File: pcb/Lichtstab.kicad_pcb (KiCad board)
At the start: 2 copper layers, 100.5 x 87.7 mm, 141 parts, among them CON1 MIKROBUS_HOST_CONN, CON2 MIKROBUS_MODULECONN, J1 RJ45_LED_Shielded, Q1 AO3407A, SW1 TS-1187A-B-A-B, SW2 TS-1187A-B-A-B, U1 ESP32-WROOM-32UE-N4, U10 HL2304, U11 LIS2DH12, U12 LIS2MDLTR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

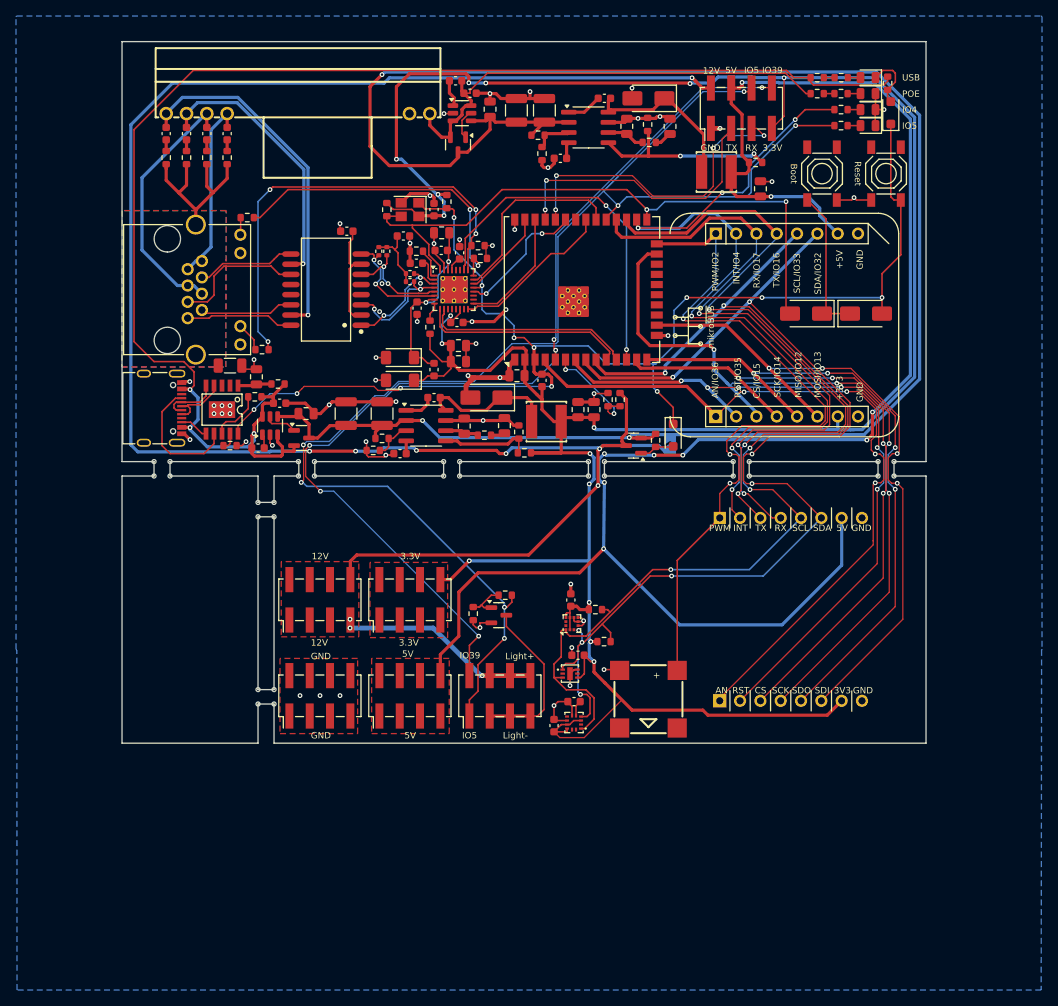
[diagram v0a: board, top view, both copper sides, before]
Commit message: 4 layer pcb
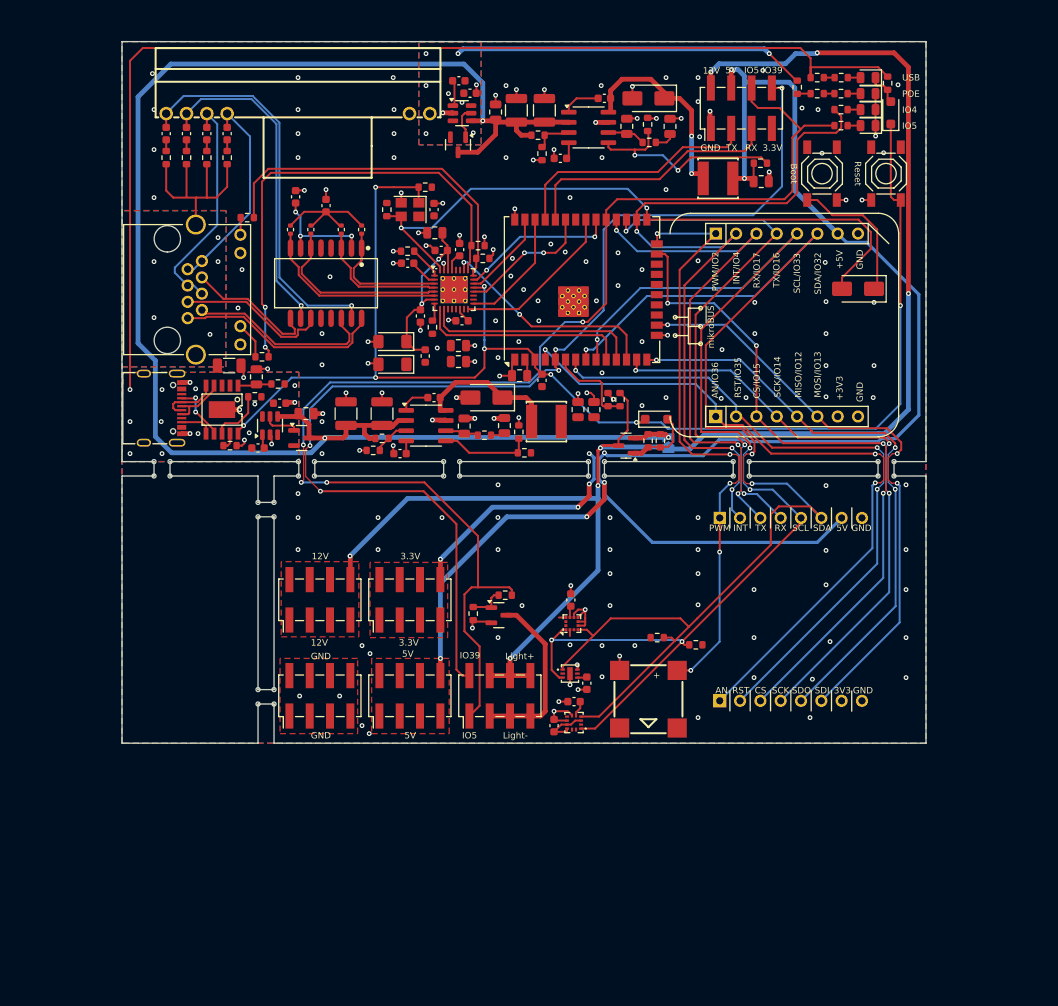
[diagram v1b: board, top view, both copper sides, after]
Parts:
- removed D1: SS34, Diode_SMD:D_SMA
- added R44: 1kΩ, Resistor_SMD:R_0603_1608Metric, F.Cu at (135.8, 98.9)
- added R45: 2.49kΩ, Resistor_SMD:R_0603_1608Metric, F.Cu at (152.9, 54.7)
- moved R41 13.3 mm to (140.2, 124.4), turned to 180 degrees
- moved R9 11.4 mm to (89.6, 72.5)
- moved R11 10.8 mm to (95.9, 72.5), turned to -90 degrees
- moved C14 10.4 mm to (94.0, 69.5), turned to -90 degrees
- moved R10 9.88 mm to (92.1, 72.5)
- moved R13 8.18 mm to (98.5, 72.5), turned to -90 degrees
- moved C11 7.71 mm to (90.2, 68.4), turned to -90 degrees
- moved D2 7.20 mm to (160.5, 79.9)
- moved R40 6.67 mm to (135.4, 123.5)
- moved C42 3.67 mm to (126.6, 129.2), turned to 90 degrees
- moved R1 3.24 mm to (106.4, 67.2), turned to 0 degrees
- moved D9 2.90 mm to (135.3, 96.2), turned to 0 degrees
- moved D5 2.21 mm to (102.3, 89.3)
- moved D6 2.21 mm to (102.3, 86.5)
- moved L2 2.02 mm to (106.4, 88.3)
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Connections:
- net USB_EN renamed /General/ESP_EN
- R34 pad 1: +12V_POE -> Net-(R34-Pad1)
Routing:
- net +3.3V: track 361.1 -> 44.6 mm, vias 16 -> 83
- net +12V: track 263.4 -> 197.0 mm, vias 10 -> 7
- net GND: track 145.0 -> 102.9 mm, vias 58 -> 102
- net +12V_USB: track 176.9 -> 141.2 mm, vias 3 -> 11
- net +12V?: track 240.0 -> 210.4 mm
- net +5V: track 220.4 -> 197.2 mm, vias 9 -> 6
- net /General/EMAC_CRS_DV: track 44.5 -> 28.2 mm
- net /General/ESP_IO39: track 126.2 -> 142.3 mm, vias 6 -> 5
- net /General/ESP_IO2: track 91.7 -> 76.0 mm, vias 3 -> 5
- net /General/ESP_IO16: track 85.3 -> 69.9 mm
- net +12V_POE: track 59.5 -> 44.3 mm, vias 0 -> 8
- net /General/ESP_IO17: track 81.4 -> 66.8 mm
- net /General/I2C_SDA: track 145.1 -> 157.2 mm, vias 8 -> 3
- net /POE/TX+: track 13.4 -> 25.2 mm
- net /POE/TX-: track 11.6 -> 22.8 mm
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- added copper zone on B.Cu, net +12V_POE
- added copper zone on F.Cu, net +12V_POE
- added copper zone on B.Cu, net +12V_USB
- added copper zone on F.Cu, net +12V_USB
- added copper zone on B.Cu, net +3.3V
- added copper zone on In1.Cu, net GND
- added copper zone on In2.Cu, net GND
- added copper zone on In1.Cu, net Net-(C4-Pad2)
- added copper zone on In2.Cu, net Net-(C4-Pad2)
- removed copper zone on B.Cu, net GND
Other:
- copper layers 2 -> 4
- board text added: "Lichtstab Module v0.4"
- board text added: "Lichtstab v0.4"
- board text removed: "Lichtstab Module v0.3"
- board text removed: "Lichtstab v0.3"

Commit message: add mounting holes
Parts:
- added REF**: MountingHole_2mm, MountingHole:MountingHole_2mm, F.Cu at (70.7, 105.5)
- added REF**: MountingHole_2mm, MountingHole:MountingHole_2mm, F.Cu at (89.7, 105.5)
- added REF**: MountingHole_2mm, MountingHole:MountingHole_2mm, F.Cu at (70.8, 51.2)
- added REF**: MountingHole_2mm, MountingHole:MountingHole_2mm, F.Cu at (160.8, 84.7)
- added REF**: MountingHole_2mm, MountingHole:MountingHole_2mm, F.Cu at (70.8, 134.4)
- added REF**: MountingHole_2mm, MountingHole:MountingHole_2mm, F.Cu at (166.2, 51.8)
- added REF**: MountingHole_2mm, MountingHole:MountingHole_2mm, F.Cu at (166.7, 134.4)
- moved D8 1.20 mm to (164.6, 59.1)
- moved R32 1.00 mm to (164.2, 55.2)
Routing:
- net +12V_USB: track 141.2 -> 139.1 mm
- net +12V: track 197.0 -> 195.4 mm
- net /General/ESP_EN: track 172.9 -> 172.2 mm
- net +3.3V: vias 83 -> 82

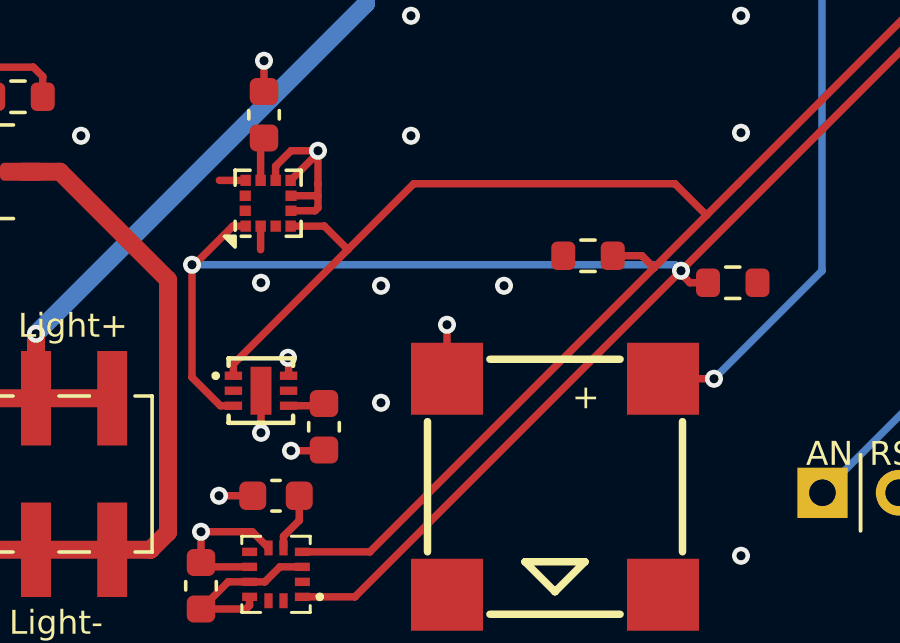
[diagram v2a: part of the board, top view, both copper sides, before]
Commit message: fix GXHTC3C pinout
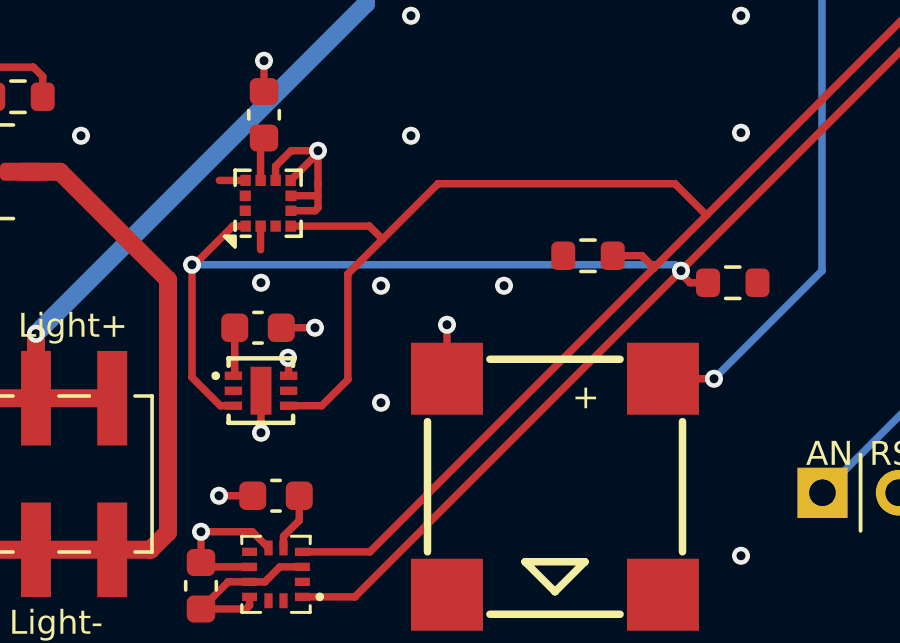
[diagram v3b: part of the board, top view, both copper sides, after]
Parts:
- moved C42 3.97 mm to (124.4, 125.9), turned to 180 degrees
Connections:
- U15 pad 1: /General/I2C_SDA -> +3.3V
- U15 pad 4: +3.3V -> /General/I2C_SDA
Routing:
- net /General/I2C_SDA: track 157.2 -> 158.6 mm
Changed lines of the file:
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@@
 			)
 		)
-		(property "Addr" "0x18"
+		(property "Addr" "0x19"
 			(at 0 0 90)
 			(unlocked yes)
@@
 			)
 		)
-		(property "Addr" "0x60"
+		(property "Addr" "0x70"
 			(at 0 0 0)
 			(unlocked yes)
@@
 			(size 0.28 0.58)
 			(layers "F.Cu" "F.Paste" "F.Mask")
-			(net 42 "/General/I2C_SDA")
-			(pinfunction "SDA")
+			(net 1 "+3.3V")
+			(pinfunction "VDD")
 			(pintype "unspecified")
 		)
@@
 			(size 0.28 0.58)
 			(layers "F.Cu" "F.Paste" "F.Mask")
-			(net 1 "+3.3V")
-			(pinfunction "VDD")
+			(net 42 "/General/I2C_SDA")
+			(pinfunction "SDA")
 			(pintype "unspecified")
 		)
@@
 			)
 		)
-		(property "Addr" "0x30"
+		(property "Addr" "0x1e"
 			(at 0 0 90)
 			(unlocked yes)
@@
 	(footprint "Capacitor_SMD:C_0603_1608Metric"
 		(layer "F.Cu")
-		(at 126.6 129.2 90)
+		(at 124.4 125.9 180)
 		(descr "Capacitor SMD 0603 (1608 Metric), square (rectangular) end terminal, IPC_7351 nominal, (Body size source: IPC-SM-782 page 76, https://www.pcb-3d.com/wordpress/wp-content/uploads/ipc-sm-782a_amendment_1_and_2.pdf), generated with kicad-footprint-generator")
 		(tags "capacitor")
 		(property "Reference" "C42"
-			(at 2.6 0 -90)
+			(at 2.6 0 180)
 			(layer "F.SilkS")
 			(hide yes)
@@
 		)
 		(property "Value" "100nF"
-			(at 0 1.43 -90)
+			(at 0 1.43 180)
 			(layer "F.Fab")
 			(effects
@@
 		)
 		(property "Footprint" "Capacitor_SMD:C_0603_1608Metric"
-			(at 0 0 90)
+			(at 0 0 180)
 			(unlocked yes)
 			(layer "F.Fab")
@@
 		)
 		(property "Datasheet" ""
-			(at 0 0 90)
+			(at 0 0 180)
 			(unlocked yes)
 			(layer "F.Fab")
@@
 		)
 		(property "Description" "Unpolarized capacitor"
-			(at 0 0 90)
+			(at 0 0 180)
 			(unlocked yes)
 			(layer "F.Fab")
@@
 		)
 		(property "LCSC" "C14663"
-			(at 0 0 90)
+			(at 0 0 180)
 			(unlocked yes)
 			(layer "F.Fab")
@@
 		(attr smd)
 		(fp_line
-			(start -0.14058 -0.51)
-			(end 0.14058 -0.51)
+			(start -0.14058 0.51)
+			(end 0.14058 0.51)
 			(stroke
 				(width 0.12)
@@
 		)
 		(fp_line
-			(start -0.14058 0.51)
-			(end 0.14058 0.51)
+			(start -0.14058 -0.51)
+			(end 0.14058 -0.51)
 			(stroke
 				(width 0.12)
@@
 		)
 		(fp_line
-			(start 1.48 -0.73)
-			(end 1.48 0.73)
+			(start 1.48 0.73)
+			(end -1.48 0.73)
 			(stroke
 				(width 0.05)
@@
 		)
 		(fp_line
-			(start -1.48 -0.73)
-			(end 1.48 -0.73)
+			(start 1.48 -0.73)
+			(end 1.48 0.73)
 			(stroke
 				(width 0.05)
@@
 		)
 		(fp_line
-			(start 1.48 0.73)
-			(end -1.48 0.73)
+			(start -1.48 0.73)
+			(end -1.48 -0.73)
 			(stroke
 				(width 0.05)
@@
 		)
 		(fp_line
-			(start -1.48 0.73)
-			(end -1.48 -0.73)
+			(start -1.48 -0.73)
+			(end 1.48 -0.73)
 			(stroke
 				(width 0.05)
@@
 		)
 		(fp_line
-			(start 0.8 -0.4)
-			(end 0.8 0.4)
+			(start 0.8 0.4)
+			(end -0.8 0.4)
 			(stroke
 				(width 0.1)
@@
 		)
 		(fp_line
-			(start -0.8 -0.4)
-			(end 0.8 -0.4)
+			(start 0.8 -0.4)
+			(end 0.8 0.4)
 			(stroke
 				(width 0.1)
@@
 		)
 		(fp_line
-			(start 0.8 0.4)
-			(end -0.8 0.4)
+			(start -0.8 0.4)
+			(end -0.8 -0.4)
 			(stroke
 				(width 0.1)
@@
 		)
 		(fp_line
-			(start -0.8 0.4)
-			(end -0.8 -0.4)
+			(start -0.8 -0.4)
+			(end 0.8 -0.4)
 			(stroke
 				(width 0.1)
@@
 		)
 		(fp_text user "${REFERENCE}"
-			(at 0 0 -90)
+			(at 0 0 180)
 			(layer "F.Fab")
 			(effects
@@
 		)
 		(pad "1" smd roundrect
-			(at -0.775 0 90)
+			(at -0.775 0 180)
 			(size 0.9 0.95)
 			(layers "F.Cu" "F.Paste" "F.Mask")
@@
 		)
 		(pad "2" smd roundrect
-			(at 0.775 0 90)
+			(at 0.775 0 180)
 			(size 0.9 0.95)
 			(layers "F.Cu" "F.Paste" "F.Mask")
@@
 	)
 	(segment
-		(start 126.525 128.5)
-		(end 126.6 128.425)
-		(width 0.25)
-		(layer "F.Cu")
-		(net 1)
-	)
-	(segment
 		(start 122.5 135.275)
 		(end 124 135.275)
@@
 	)
 	(segment
-		(start 125.42 128.5)
-		(end 126.525 128.5)
+		(start 124.12 134.37)
+		(end 123.405 134.37)
 		(width 0.25)
 		(layer "F.Cu")
@@
 	)
 	(segment
-		(start 124.12 134.37)
-		(end 123.405 134.37)
+		(start 124 135.275)
+		(end 124.12 135.155)
 		(width 0.25)
 		(layer "F.Cu")
@@
 	)
 	(segment
-		(start 124 135.275)
-		(end 124.12 135.155)
+		(start 123.625 127.455)
+		(end 123.58 127.5)
 		(width 0.25)
 		(layer "F.Cu")
@@
 	)
 	(segment
+		(start 123.625 125.9)
+		(end 123.625 127.455)
+		(width 0.25)
+		(layer "F.Cu")
+		(net 1)
+	)
+	(segment
 		(start 126.9 105.8)
 		(end 126.9 104.3)
@@
 	)
 	(segment
-		(start 125.5 130)
-		(end 126.575 130)
-		(width 0.25)
-		(layer "F.Cu")
-		(net 2)
-	)
-	(segment
 		(start 112.6 87)
 		(end 111.5 87)
@@
 	)
 	(segment
-		(start 126.575 130)
-		(end 126.6 129.975)
-		(width 0.25)
-		(layer "F.Cu")
-		(net 2)
-	)
-	(segment
 		(start 112.6 89)
 		(end 111.5 89)
@@
 	)
 	(segment
+		(start 126.3 125.9)
+		(end 125.175 125.9)
+		(width 0.25)
+		(layer "F.Cu")
+		(net 2)
+	)
+	(segment
 		(start 127.5 93.3)
 		(end 127.5 94.05)
@@
 	)
 	(via
-		(at 125.5 130)
-		(size 0.6)
-		(drill 0.3)
-		(layers "F.Cu" "B.Cu")
-		(free yes)
-		(net 2)
-	)
-	(via
 		(at 112.8 54.4)
 		(size 0.6)
@@
 	)
 	(via
+		(at 126.3 125.9)
+		(size 0.6)
+		(drill 0.3)
+		(layers "F.Cu" "B.Cu")
+		(free yes)
+		(net 2)
+	)
+	(via
 		(at 77 98)
 		(size 0.6)
@@
 	)
 	(segment
+		(start 126.525 128.5)
+		(end 127.395 127.63)
+		(width 0.25)
+		(layer "F.Cu")
+		(net 42)
+	)
+	(segment
+		(start 128.1125 122.5125)
+		(end 128.55 122.95)
+		(width 0.25)
+		(layer "F.Cu")
+		(net 42)
+	)
+	(segment
 		(start 147.552 100.248)
 		(end 147.25 100.55)
@@
 	)
 	(segment
-		(start 129.59 121.1)
-		(end 138.3 121.1)
-		(width 0.25)
-		(layer "F.Cu")
-		(net 42)
-	)
-	(segment
 		(start 150.6 107.1)
 		(end 149.6 108.1)
@@
 	)
 	(segment
-		(start 126.6125 122.5125)
-		(end 127.395 123.295)
-		(width 0.25)
-		(layer "F.Cu")
-		(net 42)
-	)
-	(segment
-		(start 138.3 121.1)
-		(end 139.35 122.15)
+		(start 125.42 128.5)
+		(end 126.525 128.5)
 		(width 0.25)
 		(layer "F.Cu")
@@
 	)
 	(segment
-		(start 126.5 87.5)
-		(end 126.5 88.73)
+		(start 127.395 124.105)
+		(end 130.4 121.1)
 		(width 0.25)
 		(layer "F.Cu")
@@
 	)
 	(segment
-		(start 127.395 123.295)
-		(end 129.59 121.1)
+		(start 126.5 87.5)
+		(end 126.5 88.73)
 		(width 0.25)
 		(layer "F.Cu")
@@
 	)
 	(segment
-		(start 125.4875 122.5125)
-		(end 126.6125 122.5125)
-		(width 0.25)
-		(layer "F.Cu")
-		(net 42)
-	)
-	(segment
-		(start 123.58 127.5)
-		(end 123.58 127.11)
+		(start 141.5 97.3)
+		(end 145.9 97.3)
 		(width 0.25)
 		(layer "F.Cu")
@@
 	)
 	(segment
-		(start 141.5 97.3)
-		(end 145.9 97.3)
+		(start 127.395 127.63)
+		(end 127.395 124.105)
 		(width 0.25)
 		(layer "F.Cu")
@@
 	)
 	(segment
-		(start 123.58 127.11)
-		(end 127.395 123.295)
+		(start 138.3 121.1)
+		(end 139.35 122.15)
 		(width 0.25)
 		(layer "F.Cu")
@@
 	)
 	(segment
+		(start 130.4 121.1)
+		(end 138.3 121.1)
+		(width 0.25)
+		(layer "F.Cu")
+		(net 42)
+	)
+	(segment
 		(start 137.6 123.9)
 		(end 128.13 133.37)
@@
 	)
 	(segment
+		(start 125.4875 122.5125)
+		(end 128.1125 122.5125)
+		(width 0.25)
+		(layer "F.Cu")
+		(net 42)
+	)
+	(segment
 		(start 128.13 133.37)
 		(end 125.88 133.37)
@@
 		(polygon
 			(pts
-				(xy 125 128.2) (xy 125.9 128.2) (xy 125.9 128.8) (xy 125 128.8)
+				(xy 123.1 127.2) (xy 124 127.2) (xy 124 127.8) (xy 123.1 127.8)
 			)
 		)
